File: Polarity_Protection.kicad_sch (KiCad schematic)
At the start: 5 parts, among them J1 IN+, J2 IN-, Q1 BSS214NW

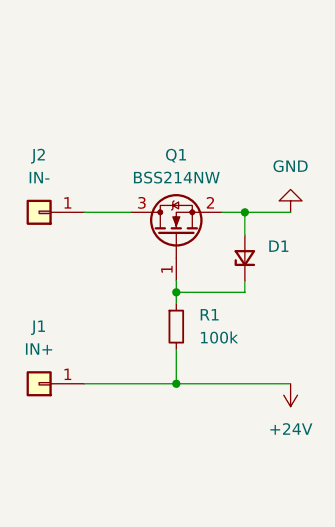
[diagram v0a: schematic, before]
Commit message: Поставил керамические Y конденсаторы
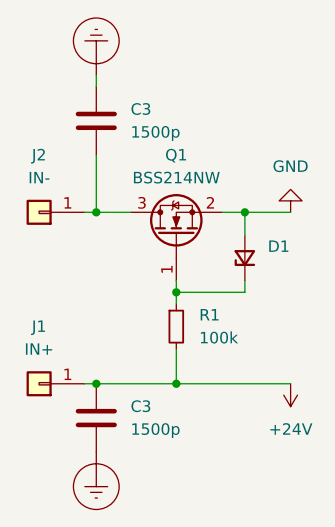
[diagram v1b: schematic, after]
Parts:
- added C3 (x2): 1500p, Capacitor_THT:C_Disc_D7.5mm_W5.0mm_P7.50mm, symbol Device:C
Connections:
- net +24V: now also C3.1
- net at J2.1 (Pin_1), Q1.3 (D): now also C3.2
- new net Earth_Protective: C3.1, C3.2
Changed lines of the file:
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@@
   (junction (at 142.24 104.14) (diameter 0) (color 0 0 0 0)
   )
+  (junction (at 133.35 104.14) (diameter 0) (color 0 0 0 0)
+  )
   (junction (at 149.86 85.09) (diameter 0) (color 0 0 0 0)
   )
   (junction (at 142.24 93.98) (diameter 0) (color 0 0 0 0)
   )
-  (wire (pts (xy 132.08 85.09) (xy 137.16 85.09))
+  (junction (at 133.35 85.09) (diameter 0) (color 0 0 0 0)
+  )
+  (wire (pts (xy 132.08 85.09) (xy 133.35 85.09))
+    (stroke (width 0) (type default))
+  )
+  (wire (pts (xy 133.35 85.09) (xy 137.16 85.09))
     (stroke (width 0) (type default))
   )
@@
     (stroke (width 0) (type default))
   )
+  (wire (pts (xy 133.35 78.74) (xy 133.35 85.09))
+    (stroke (width 0) (type default))
+  )
   (wire (pts (xy 149.86 92.71) (xy 149.86 93.98))
     (stroke (width 0) (type default))
@@
     (stroke (width 0) (type default))
   )
-  (wire (pts (xy 132.08 104.14) (xy 142.24 104.14))
+  (wire (pts (xy 133.35 104.14) (xy 142.24 104.14))
+    (stroke (width 0) (type default))
+  )
+  (wire (pts (xy 132.08 104.14) (xy 133.35 104.14))
     (stroke (width 0) (type default))
   )
@@
     (stroke (width 0) (type default))
   )
+  (wire (pts (xy 133.35 69.85) (xy 133.35 71.12))
+    (stroke (width 0) (type default))
+  )
   (symbol (lib_id "Device:R_Small") (at 142.24 97.79 0) (unit 1)
     (in_bom yes) (on_board yes) (dnp no) (fields_autoplaced)
@@
       (project "Силовая плата"
         (path "/96c6fc92-8ec6-44f7-b0dc-9ad8f1acea09/1efb5faf-bb82-4ac6-a144-d6576b4720aa"
-          (reference "J9") (unit 1)
+          (reference "J5") (unit 1)
+        )
+      )
+    )
+  )
+  (symbol (lib_id "power:Earth_Protective") (at 133.35 111.76 0) (unit 1)
+    (in_bom yes) (on_board yes) (dnp no) (fields_autoplaced)
+    (property "Reference" "#PWR010" (at 139.7 118.11 0)
+      (effects (font (size 1.27 1.27)) hide)
+    )
+    (property "Value" "Earth_Protective" (at 144.78 115.57 0)
+      (effects (font (size 1.27 1.27)) hide)
+    )
+    (property "Footprint" "" (at 133.35 114.3 0)
+      (effects (font (size 1.27 1.27)) hide)
+    )
+    (property "Datasheet" "~" (at 133.35 114.3 0)
+      (effects (font (size 1.27 1.27)) hide)
+    )
+    (pin "1")
+    (instances
+      (project "Силовая плата"
+        (path "/96c6fc92-8ec6-44f7-b0dc-9ad8f1acea09/c8b8118a-2e72-42b0-9c26-f9b5e594da69"
+          (reference "#PWR010") (unit 1)
+        )
+        (path "/96c6fc92-8ec6-44f7-b0dc-9ad8f1acea09/1efb5faf-bb82-4ac6-a144-d6576b4720aa"
+          (reference "#PWR010") (unit 1)
         )
       )
@@
       (project "Силовая плата"
         (path "/96c6fc92-8ec6-44f7-b0dc-9ad8f1acea09/1efb5faf-bb82-4ac6-a144-d6576b4720aa"
-          (reference "J8") (unit 1)
+          (reference "J4") (unit 1)
+        )
+      )
+    )
+  )
+  (symbol (lib_id "Device:C") (at 133.35 107.95 0) (unit 1)
+    (in_bom yes) (on_board yes) (dnp no) (fields_autoplaced)
+    (property "Reference" "C3" (at 137.16 106.68 0)
+      (effects (font (size 1.27 1.27)) (justify left))
+    )
+    (property "Value" "1500p" (at 137.16 109.22 0)
+      (effects (font (size 1.27 1.27)) (justify left))
+    )
+    (property "Footprint" "Capacitor_THT:C_Disc_D7.5mm_W5.0mm_P7.50mm" (at 134.3152 111.76 0)
+      (effects (font (size 1.27 1.27)) hide)
+    )
+    (property "Datasheet" "~" (at 133.35 107.95 0)
+      (effects (font (size 1.27 1.27)) hide)
+    )
+    (pin "1")
+    (pin "2")
+    (instances
+      (project "Силовая плата"
+        (path "/96c6fc92-8ec6-44f7-b0dc-9ad8f1acea09"
+          (reference "C3") (unit 1)
+        )
+        (path "/96c6fc92-8ec6-44f7-b0dc-9ad8f1acea09/c8b8118a-2e72-42b0-9c26-f9b5e594da69"
+          (reference "C5") (unit 1)
+        )
+        (path "/96c6fc92-8ec6-44f7-b0dc-9ad8f1acea09/1efb5faf-bb82-4ac6-a144-d6576b4720aa"
+          (reference "C5") (unit 1)
         )
       )
@@
       (project "Силовая плата"
         (path "/96c6fc92-8ec6-44f7-b0dc-9ad8f1acea09/1efb5faf-bb82-4ac6-a144-d6576b4720aa"
-          (reference "#PWR010") (unit 1)
+          (reference "#PWR015") (unit 1)
+        )
+      )
+    )
+  )
+  (symbol (lib_id "power:Earth_Protective") (at 133.35 69.85 180) (unit 1)
+    (in_bom yes) (on_board yes) (dnp no) (fields_autoplaced)
+    (property "Reference" "#PWR09" (at 127 63.5 0)
+      (effects (font (size 1.27 1.27)) hide)
+    )
+    (property "Value" "Earth_Protective" (at 121.92 66.04 0)
+      (effects (font (size 1.27 1.27)) hide)
+    )
+    (property "Footprint" "" (at 133.35 67.31 0)
+      (effects (font (size 1.27 1.27)) hide)
+    )
+    (property "Datasheet" "~" (at 133.35 67.31 0)
+      (effects (font (size 1.27 1.27)) hide)
+    )
+    (pin "1")
+    (instances
+      (project "Силовая плата"
+        (path "/96c6fc92-8ec6-44f7-b0dc-9ad8f1acea09/c8b8118a-2e72-42b0-9c26-f9b5e594da69"
+          (reference "#PWR09") (unit 1)
+        )
+        (path "/96c6fc92-8ec6-44f7-b0dc-9ad8f1acea09/1efb5faf-bb82-4ac6-a144-d6576b4720aa"
+          (reference "#PWR09") (unit 1)
         )
       )
@@
         )
         (path "/96c6fc92-8ec6-44f7-b0dc-9ad8f1acea09/1efb5faf-bb82-4ac6-a144-d6576b4720aa"
-          (reference "#PWR011") (unit 1)
+          (reference "#PWR016") (unit 1)
         )
       )
@@
         )
       )
+    )
+  )
+  (symbol (lib_id "Device:C") (at 133.35 74.93 0) (unit 1)
+    (in_bom yes) (on_board yes) (dnp no) (fields_autoplaced)
+    (property "Reference" "C3" (at 137.16 73.66 0)
+      (effects (font (size 1.27 1.27)) (justify left))
+    )
+    (property "Value" "1500p" (at 137.16 76.2 0)
+      (effects (font (size 1.27 1.27)) (justify left))
+    )
+    (property "Footprint" "Capacitor_THT:C_Disc_D7.5mm_W5.0mm_P7.50mm" (at 134.3152 78.74 0)
+      (effects (font (size 1.27 1.27)) hide)
+    )
+    (property "Datasheet" "~" (at 133.35 74.93 0)
+      (effects (font (size 1.27 1.27)) hide)
+    )
+    (pin "1")
+    (pin "2")
+    (instances
+      (project "Силовая плата"
+        (path "/96c6fc92-8ec6-44f7-b0dc-9ad8f1acea09"
+          (reference "C3") (unit 1)
+        )
+        (path "/96c6fc92-8ec6-44f7-b0dc-9ad8f1acea09/c8b8118a-2e72-42b0-9c26-f9b5e594da69"
+          (reference "C4") (unit 1)
+        )
+        (path "/96c6fc92-8ec6-44f7-b0dc-9ad8f1acea09/1efb5faf-bb82-4ac6-a144-d6576b4720aa"
+          (reference "C4") (unit 1)
+        )
+      )

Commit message: Добавил документы
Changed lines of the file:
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@@
   (symbol (lib_id "Device:R_Small") (at 142.24 97.79 0) (unit 1)
     (in_bom yes) (on_board yes) (dnp no) (fields_autoplaced)
-    (property "Reference" "R1" (at 144.78 96.52 0)
+    (property "Reference" "R1" (at 144.78 97.155 0)
       (effects (font (size 1.27 1.27)) (justify left))
     )
-    (property "Value" "100k" (at 144.78 99.06 0)
+    (property "Value" "100k" (at 144.78 99.695 0)
       (effects (font (size 1.27 1.27)) (justify left))
     )
@@
       (project "Силовая плата"
         (path "/96c6fc92-8ec6-44f7-b0dc-9ad8f1acea09/1efb5faf-bb82-4ac6-a144-d6576b4720aa"
-          (reference "R3") (unit 1)
+          (reference "R2") (unit 1)
         )
       )
